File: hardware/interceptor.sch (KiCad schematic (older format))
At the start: 34 parts, among them IC1 ATMEGA1284P-P, K1 USB, P1 TAPEPORT, P2 CIA1, P3 KEYBOARD, P4 USER, SW1 RESET, SW2 BOOTLOADER, U1 7400, U2 ICL7660, U3 4520, U4 4051, U5 4051, U6 CD74HC22106, X1 16Mhz

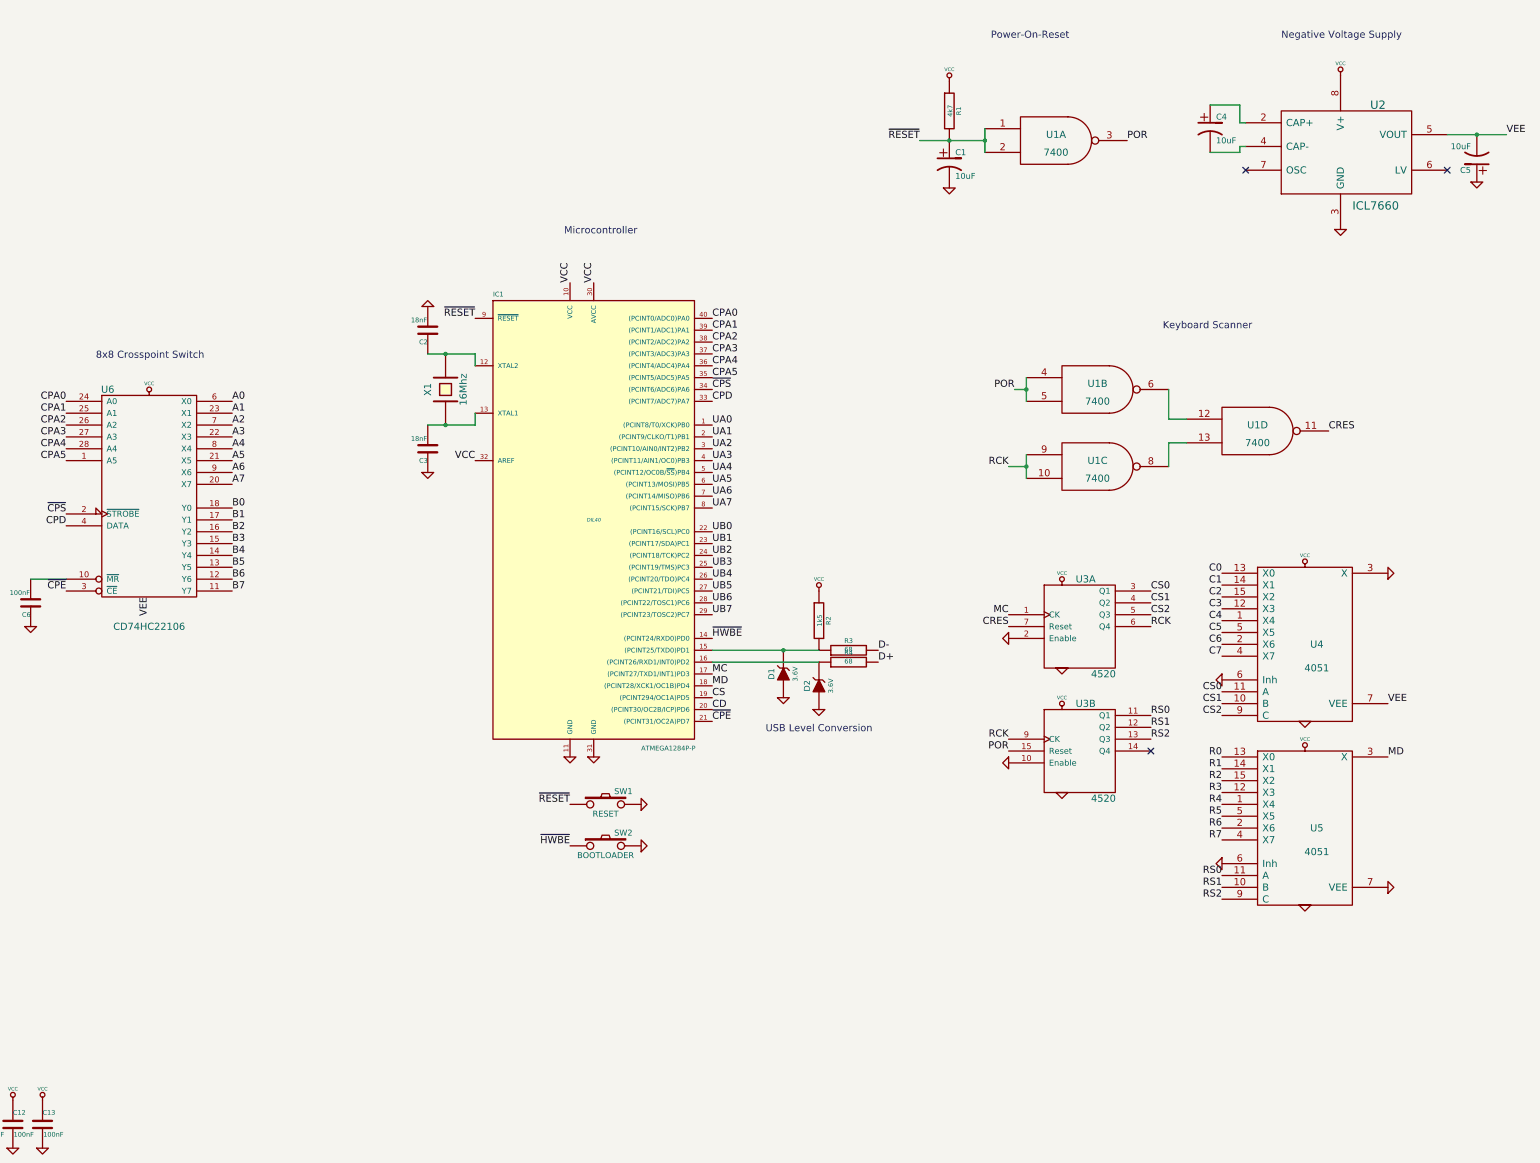
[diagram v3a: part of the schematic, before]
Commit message: Also use HWBE line as matrix reset line, reset before each scan
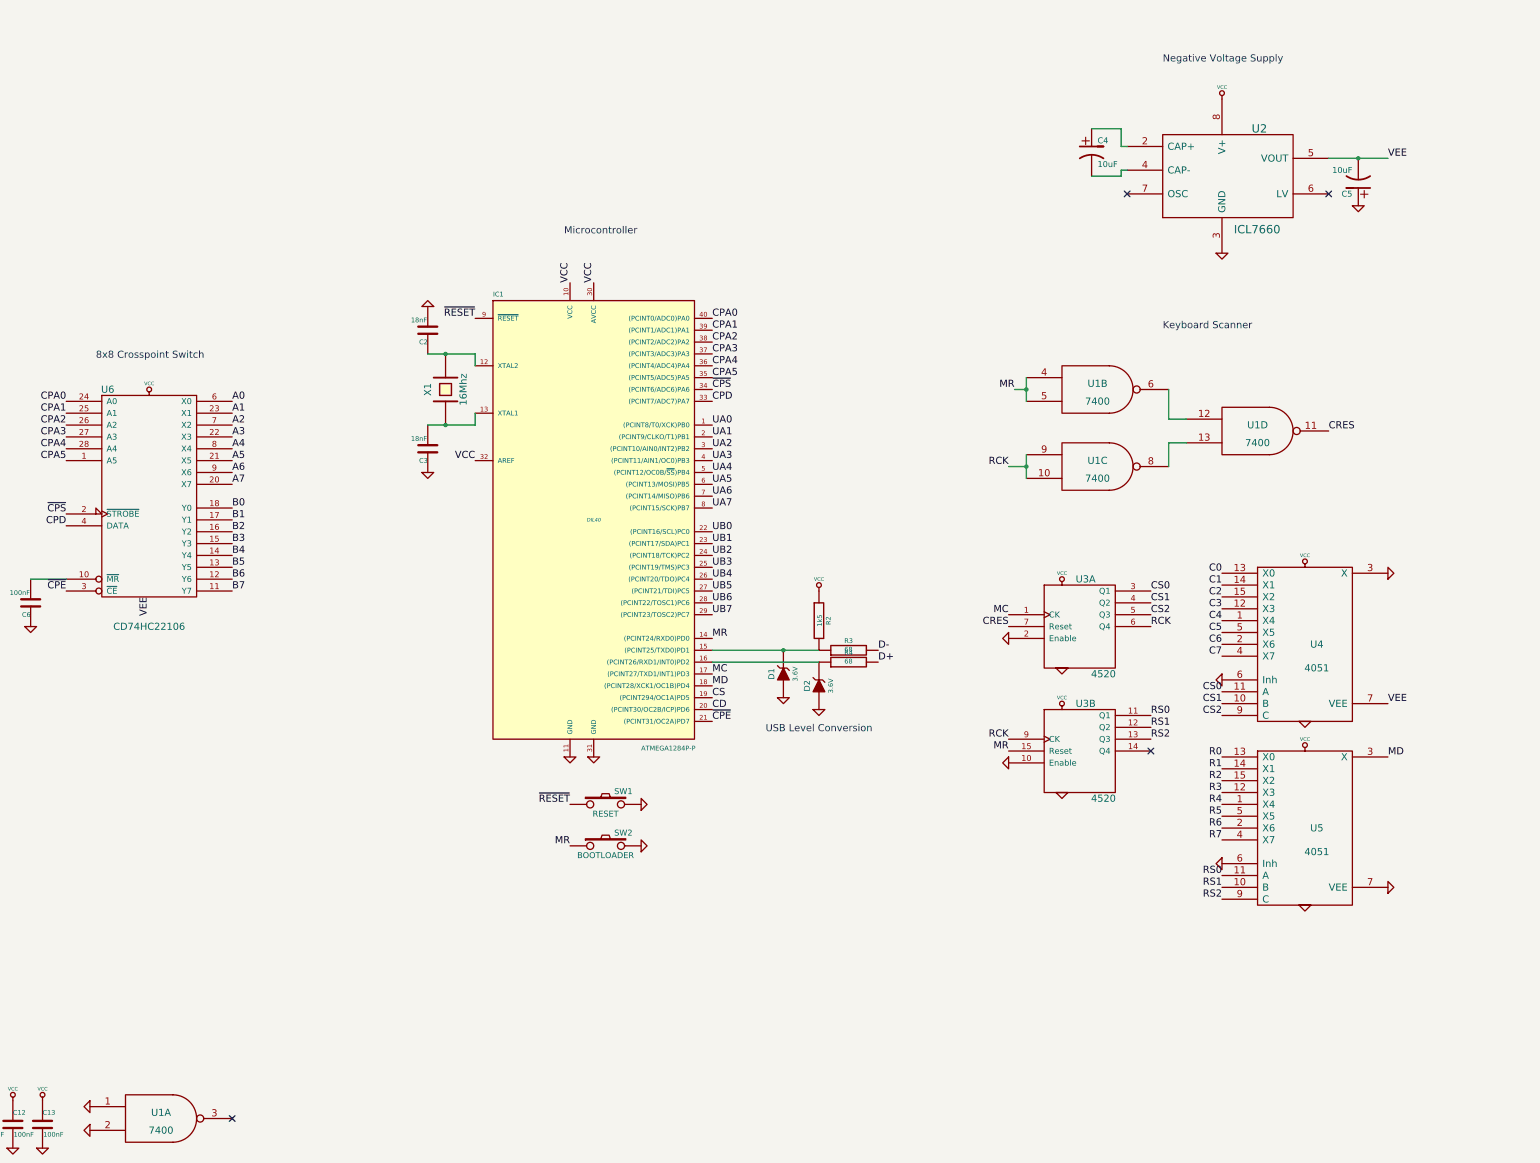
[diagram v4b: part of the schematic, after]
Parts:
- removed C1: 10uF, ~, symbol CP1
- removed R1: 4k7, ~, symbol R
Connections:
- net ~HWBE is gone; now on net MR: IC1.14 ((PCINT24/RXD0)PD0), SW2.1
- net GND: now also U1.1, U1.2
- net ~RESET: no longer U1.1, U1.2
- net POR renamed MR
- net MR: no longer U1.3
- no-connect marks 5 -> 6
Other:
- note removed: "Power-On-Reset\n"
- moved on the sheet: C4, C5, U1A, U2

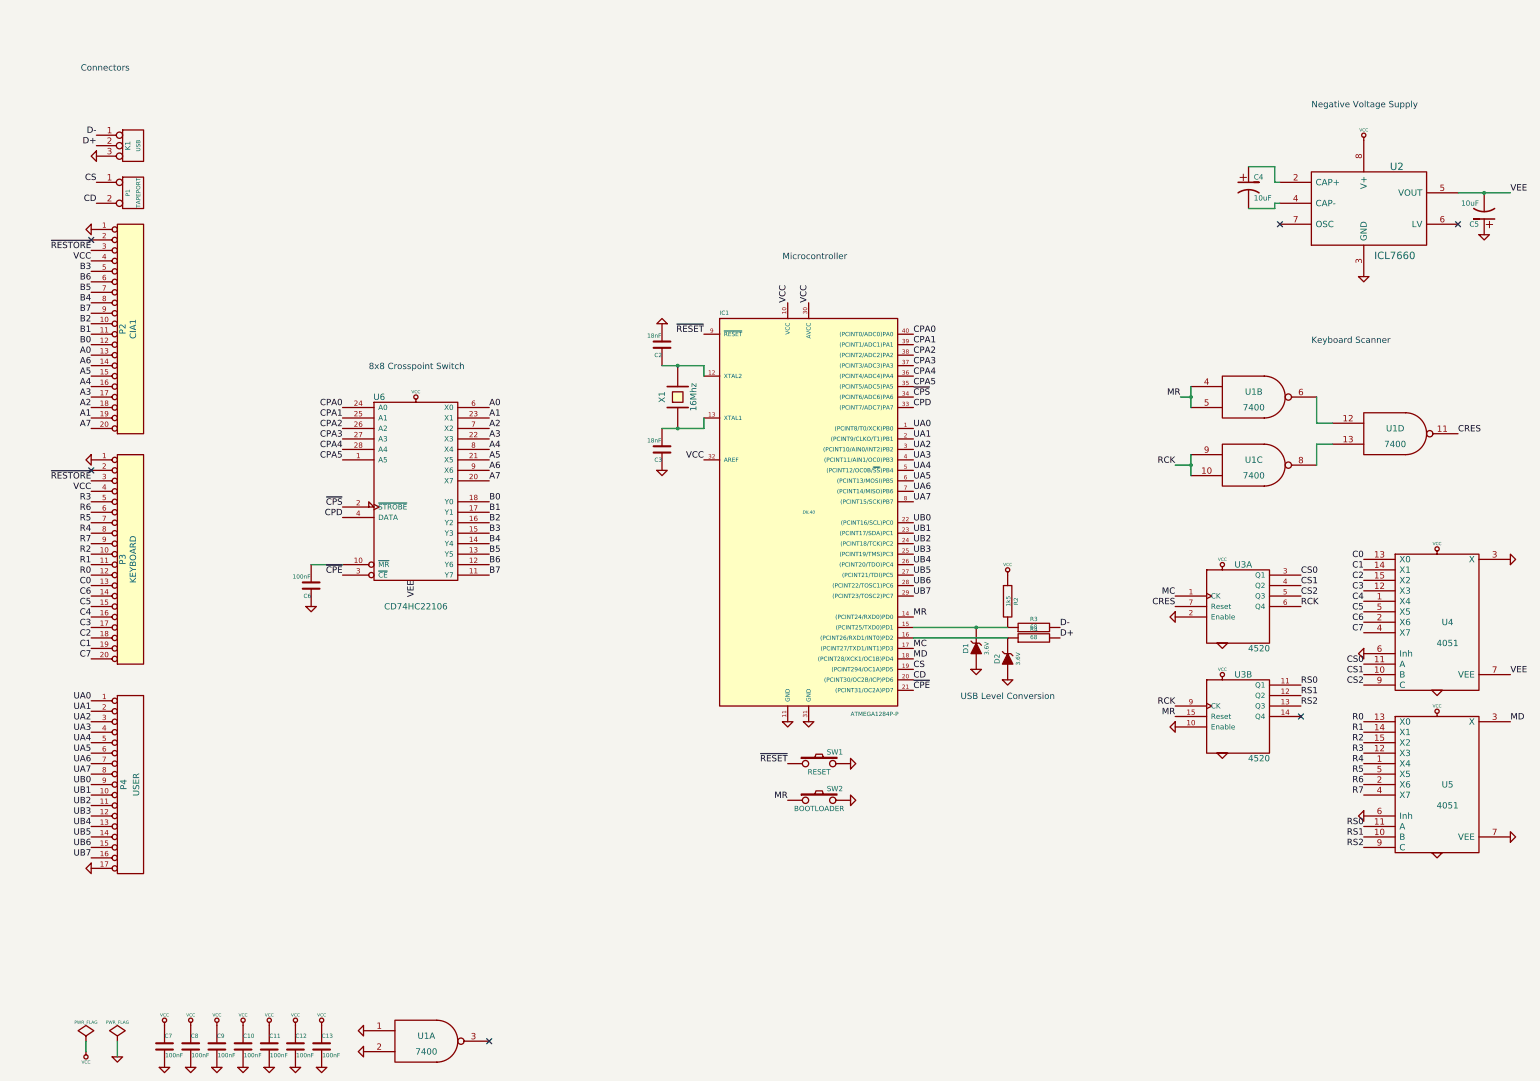
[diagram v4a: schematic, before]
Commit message: Hardware: Rearranged schematics
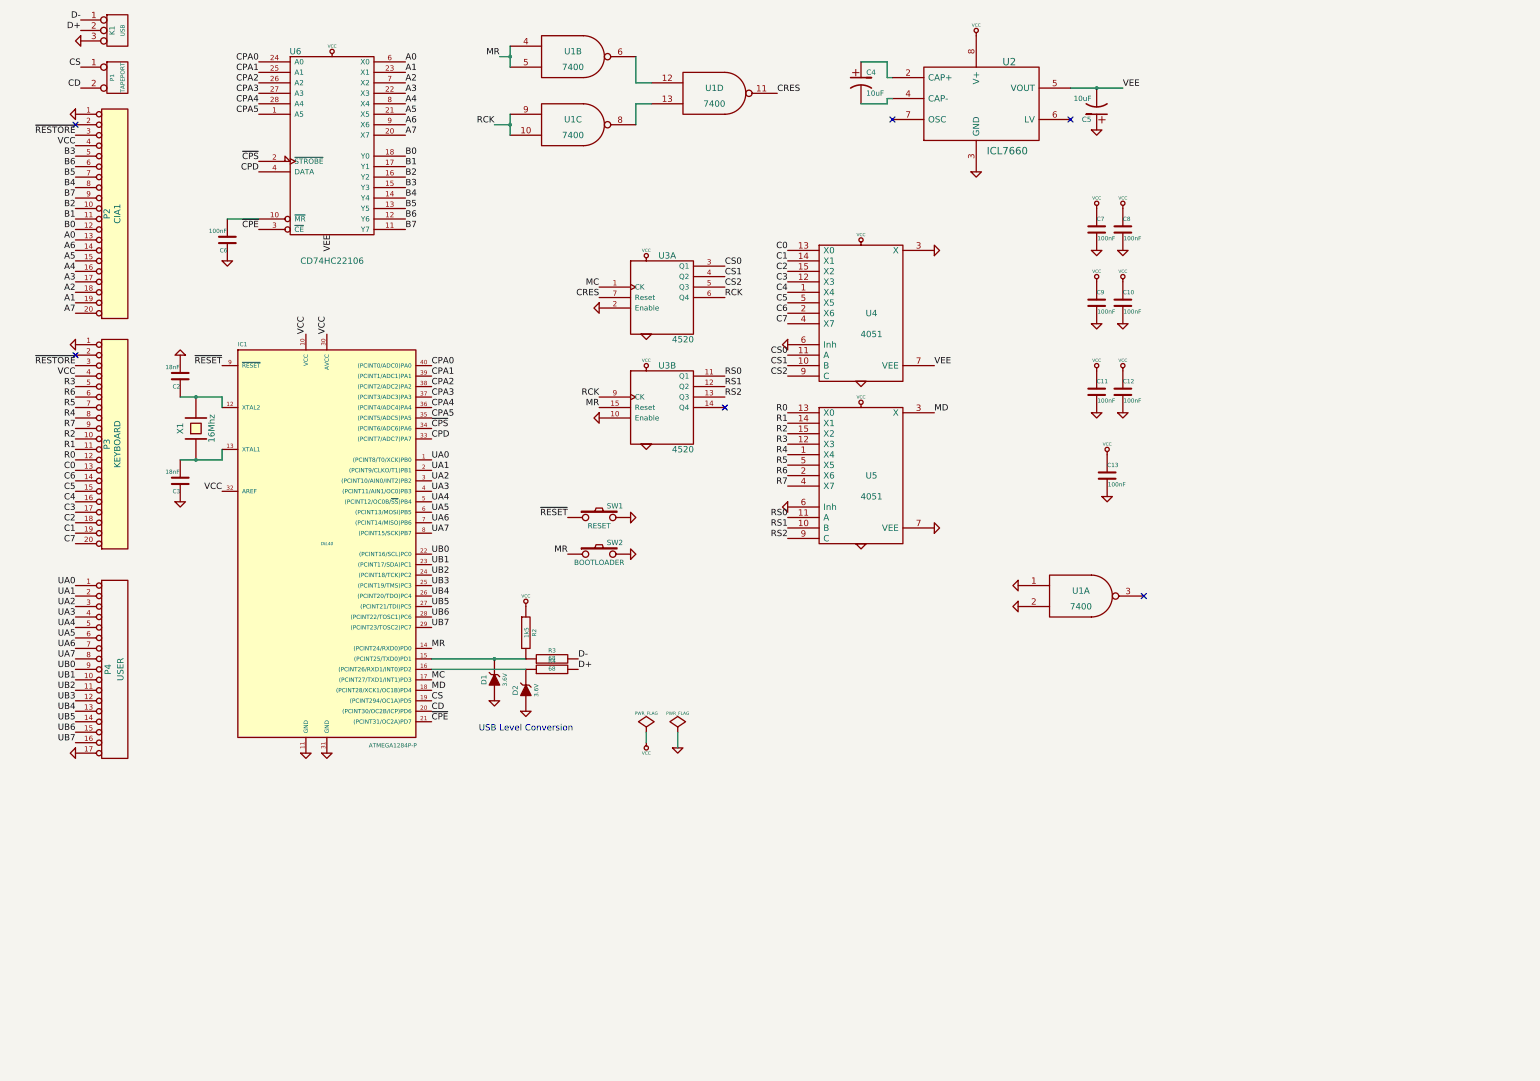
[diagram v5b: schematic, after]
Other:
- note removed: "8x8 Crosspoint Switch"
- note removed: "Connectors"
- note removed: "Keyboard Scanner"
- note removed: "Microcontroller"
- note removed: "Negative Voltage Supply\n"
- moved on the sheet: C10, C11, C12, C13, C2, C3, C4, C5, C6, C7, C8, C9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

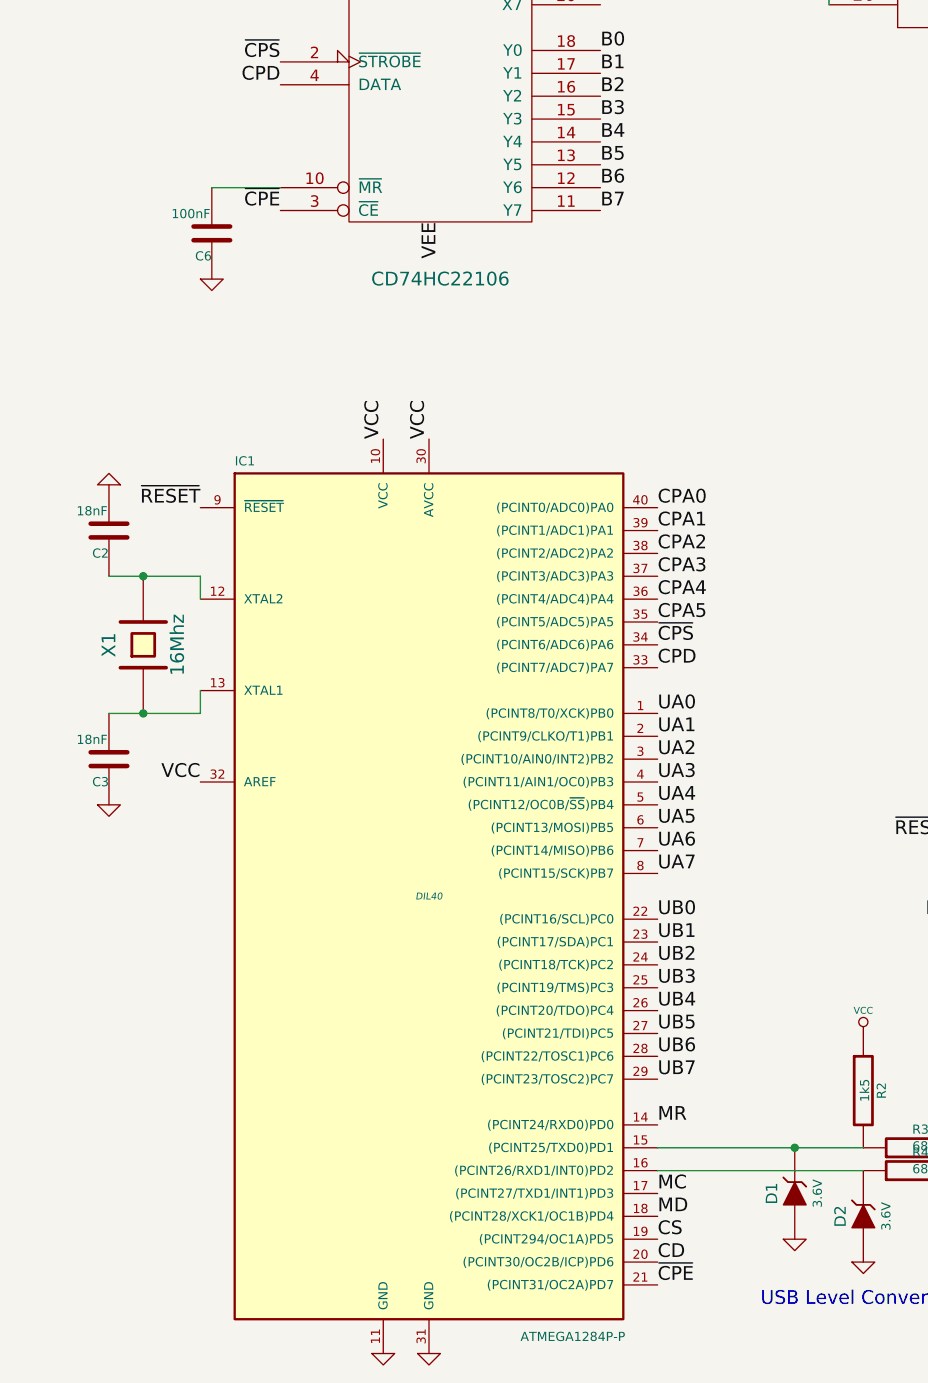
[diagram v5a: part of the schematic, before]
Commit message: Grounded crosspoint enable, connected master reset to uC
Master Reset line is more suitable to make the matrix "float"
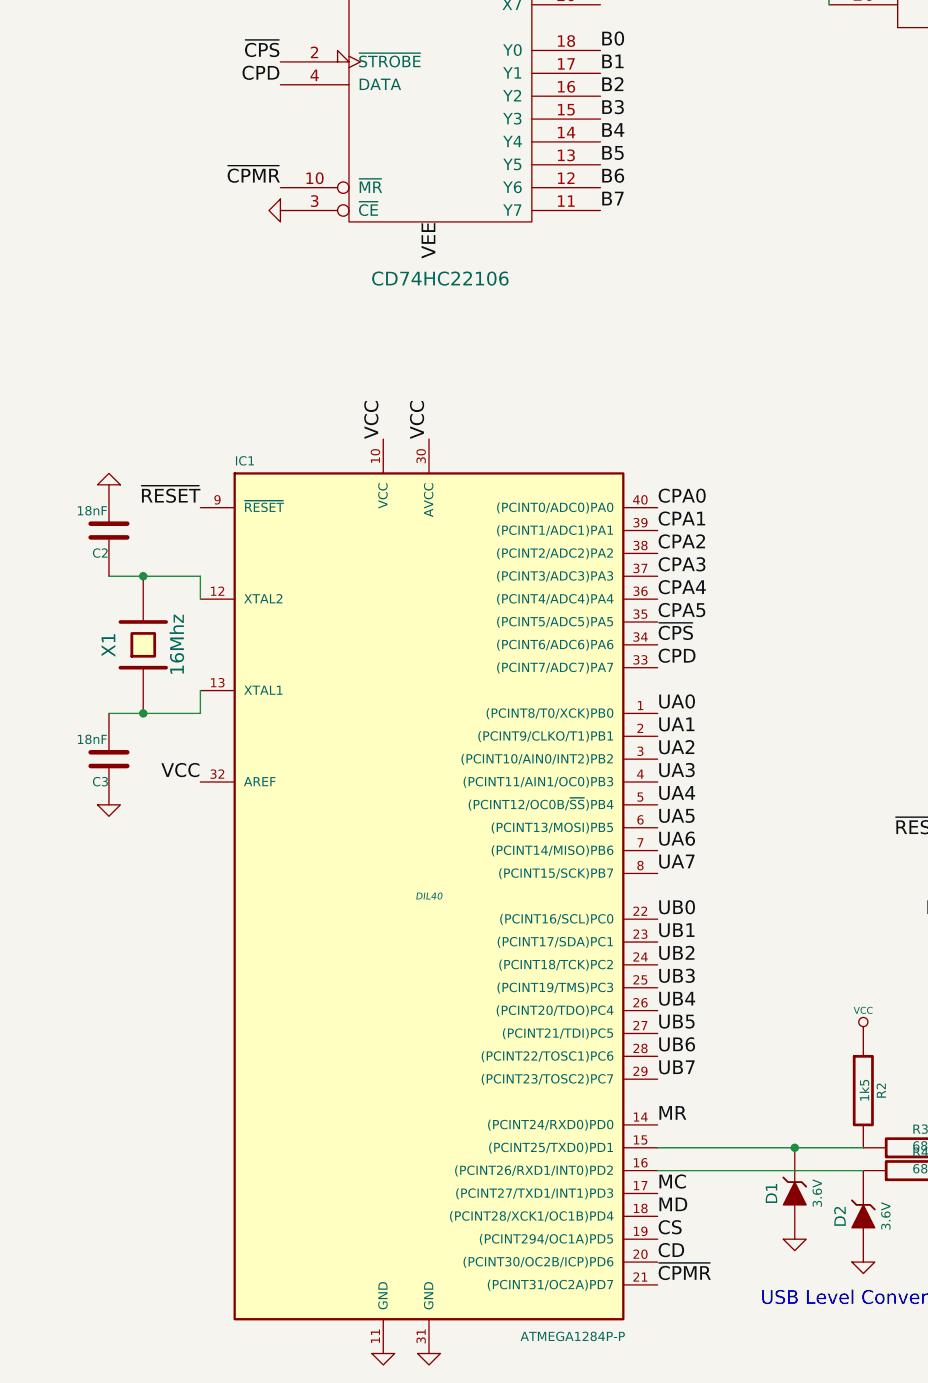
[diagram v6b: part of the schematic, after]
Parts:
- removed C6: 100nF, symbol C
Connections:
- net GND: now also U6.3 (~CE)
- net ~CPMR: now reaches U6.10 (~MR)
- net ~CPMR: now also IC1.21 ((PCINT31/OC2A)PD7)
- removed net ~CPE: IC1.21 ((PCINT31/OC2A)PD7), U6.3 (~CE)
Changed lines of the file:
@@
 Text Label 3350 2650 3    60   ~ 0
 VEE
-$Comp
-L C C6
-U 1 1 55B375C0
-P 2350 2700
-F 0 "C6" H 2350 2800 40  0000 L CNN
-F 1 "100nF" H 2356 2615 40  0000 L CNN
-F 2 "" H 2388 2550 30  0000 C CNN
-F 3 "" H 2350 2700 60  0000 C CNN
-	1    2350 2700
-	-1   0    0    1
-$EndComp
-Wire Wire Line
-	2350 2500 2650 2500
-$Comp
-L GND #PWR041
-U 1 1 55B37604
-P 2350 2900
-F 0 "#PWR041" H 2350 2900 30  0001 C CNN
-F 1 "GND" H 2350 2830 30  0001 C CNN
-F 2 "" H 2350 2900 60  0000 C CNN
-F 3 "" H 2350 2900 60  0000 C CNN
-	1    2350 2900
-	1    0    0    -1
-$EndComp
 Text Label 2650 1000 2    60   ~ 0
 CPA0
@@
 Text Label 2650 2050 2    60   ~ 0
 CPD
-Text Label 2650 2600 2    60   ~ 0
-~CPE
 Text Label 4300 3900 0    60   ~ 0
 CPA0
@@
 Text Label 4300 4600 0    60   ~ 0
 CPD
-Text Label 4300 7300 0    60   ~ 0
-~CPE
 $Comp
 L GND #PWR042
@@
 Text Label 5900 4300 2    60   ~ 0
 MR
+$Comp
+L GND #PWR?
+U 1 1 55B68DDD
+P 2650 2600
+F 0 "#PWR?" H 2650 2600 30  0001 C CNN
+F 1 "GND" H 2650 2530 30  0001 C CNN
+F 2 "" H 2650 2600 60  0000 C CNN
+F 3 "" H 2650 2600 60  0000 C CNN
+	1    2650 2600
+	0    1    1    0
+$EndComp
+Text Label 2650 2500 2    60   ~ 0
+~CPMR
+Text Label 4300 7300 0    60   ~ 0
+~CPMR
 $EndSCHEMATC
